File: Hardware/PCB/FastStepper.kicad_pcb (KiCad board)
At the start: 4 copper layers, 58 x 77.6 mm, 126 parts, among them IC1 FT232RL, IC10 THS4281DBVT, IC11 M74VHC1GT126DT1G, IC13 M74VHC1GT126DT1G, IC14 M74VHC1GT126DT1G, IC15 M74VHC1GT126DT1G, IC16 M74VHC1GT126DT1G, IC17 M74VHC1GT126DT1G, IC18 M74VHC1GT126DT1G, IC19 M74VHC1GT126DT1G, IC2 M74VHC1GT126DT1G, IC20 M74VHC1GT126DT1G, IC21 M74VHC1GT126DT1G, IC22 M74VHC1GT126DT1G, IC3 LP5907MFX-3.3, IC4 M74VHC1GT126DT1G, IC5 M74VHC1GT126DT1G, IC6 M74VHC1GT126DT1G, IC8 ATXMEGA32A4U, J1 USB_C_Receptacle, J2 AudioJack3_Ground_SwitchTR, J3 AudioJack3_Ground_SwitchTR, Q1 AO3401A, U1 74LVC1G157, U2 THVD1450D, U3 ADuM1201BR NOT NORMALLY STOCK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, X1 conn 1x5 2, X10 conn 1x3, X2 conn 1x5, X3 conn 1x2, X4 conn 1x3, X5 conn 1x5, X6 OSCILLATOR, X9 conn 1x5

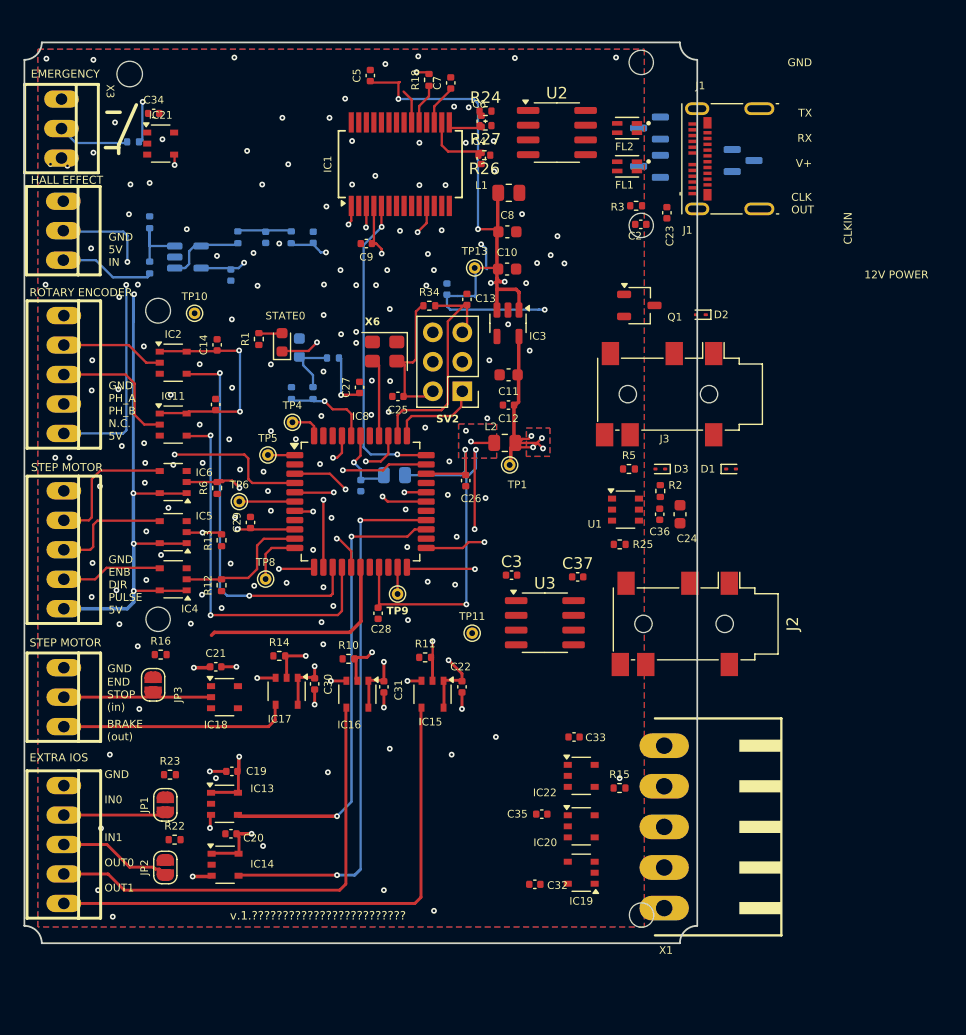
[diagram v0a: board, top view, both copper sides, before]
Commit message: FastStepper DRC=0
DRC=0
ainda não revisto com mais ninguém
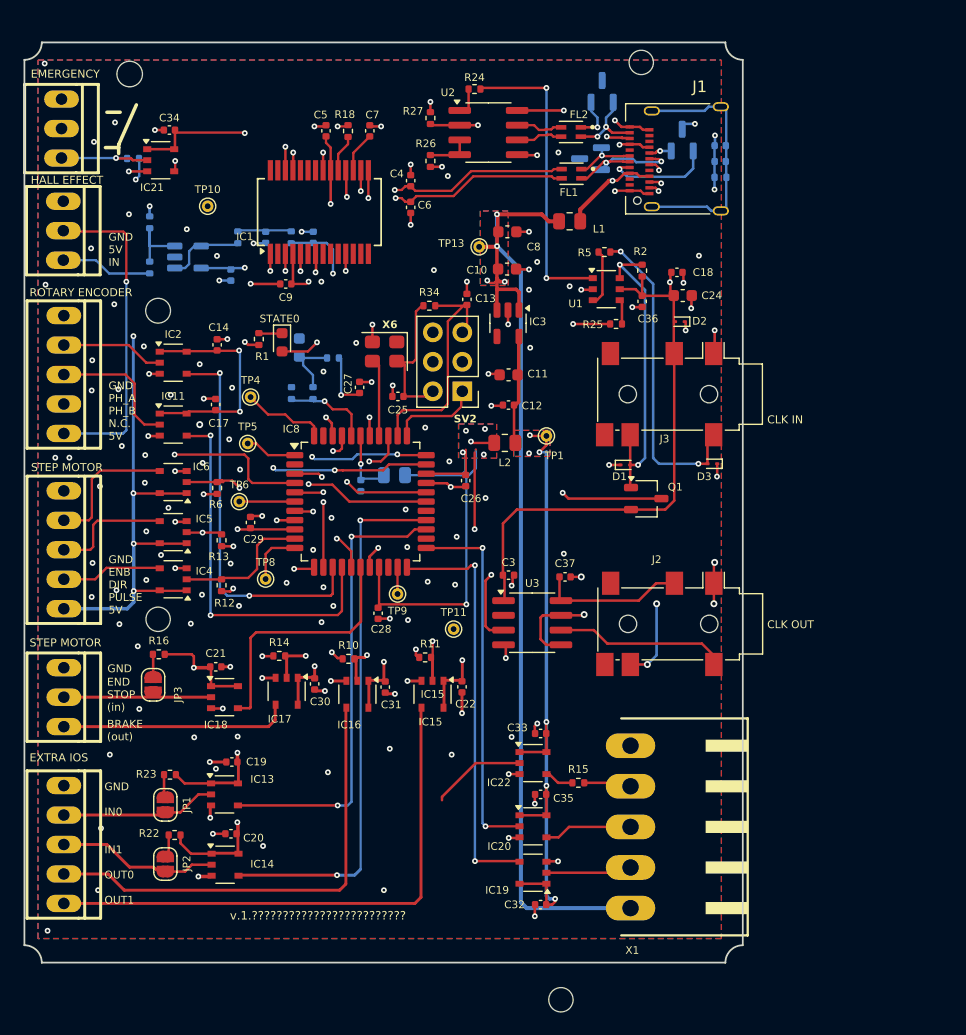
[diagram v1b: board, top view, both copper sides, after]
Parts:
- C18: moved to F.Cu
- C2, C23, R3: moved to B.Cu
- J1: footprint Connector_USB:USB_C_Receptacle_Molex_105450-0101 -> Connector_USB:USB_C_Receptacle_Amphenol_12401610E4-2A
- moved C18 19.9 mm to (175.8, 86.0), turned to 180 degrees
- moved U1 19.1 mm to (169.7, 87.5)
- moved R2 19.1 mm to (172.8, 85.8)
- moved R25 19.0 mm to (170.5, 90.5)
- moved C24 18.9 mm to (176.2, 88.0), turned to 0 degrees
- moved R5 18.8 mm to (169.5, 84.2)
- moved C36 18.4 mm to (172.8, 88.5)
- moved Q1 16.7 mm to (173.1, 105.5)
- moved C6 9.60 mm to (152.8, 80.4), turned to -90 degrees
- moved TP10 9.30 mm to (135.3, 80.3)
- moved D1 9.12 mm to (171.3, 102.6)
- moved C2 8.73 mm to (179.5, 76.4), turned to 180 degrees
- moved R18 8.26 mm to (147.4, 73.8)
- moved C7 8.11 mm to (149.3, 73.8)
- moved IC1 8.11 mm to (144.9, 80.8)
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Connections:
- net Net-(D3-A2) renamed /Clock stage/CLCK_IN
- net Net-(U3-VOB) renamed /Clock stage/CLCK_OUT
- C18 pad 2: Net-(D2-A2) -> VClk
- D2 pad 2: Net-(D2-A2) -> VClk
- D4 pad 1: /CC2 -> /CC1
- D4 pad 2: /CC1 -> /CC2
- FL1 pad 1: /USB_P -> /USB_N
- FL1 pad 2: /USB_2u_P -> /USB_2u_N
- FL1 pad 3: /USB_2u_N -> /USB_2u_P
- FL1 pad 4: /USB_N -> /USB_P
- J3 pad 3: Net-(D2-A2) -> VClk
- R27 pad 1: Net-(U2-~{RE}) -> ~{CLK_EN_USB}
- U2 pad 2: Net-(U2-~{RE}) -> ~{CLK_EN_USB}
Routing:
- net GND: track 12.9 -> 103.2 mm, vias 141 -> 150
- net VClk: track 0.00 -> 76.0 mm, vias 0 -> 3
- net +5V: track 245.0 -> 313.9 mm
- net ~{CLK_EN_USB}: track 0.00 -> 51.1 mm, vias 0 -> 3
- net GNDS: track 0.00 -> 42.8 mm, vias 0 -> 6
- net HARP_H2_RX: track 5.88 -> 35.3 mm, vias 1 -> 2
- net +3V3: track 272.8 -> 300.9 mm, vias 18 -> 21
- net /Clock stage/CLCK_IN: track 0.00 -> 27.6 mm, vias 0 -> 2
- net Net-(D1-A2): track 0.00 -> 26.8 mm, vias 0 -> 2
- net HARP_H2_TX: track 5.10 -> 31.8 mm, vias 1 -> 2
- net CLK_USB: track 0.00 -> 26.0 mm, vias 0 -> 2
- net Net-(J1-SHIELD): track 0.00 -> 21.2 mm
- net /USB_2u_P: track 3.43 -> 20.3 mm, vias 0 -> 2
- net /USB_CLCK_P: track 0.00 -> 16.4 mm, vias 0 -> 3
- net /USB_CLCK_N: track 0.00 -> 15.4 mm, vias 0 -> 3
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- added copper zone on B.Cu, net +5V
- added copper zone on F.Cu, net +5V
- added copper zone on In1.Cu, net +5V
- added copper zone on In2.Cu, net +5V
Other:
- board size 58 x 77.6 mm -> 61.9 x 83.6 mm
- board text added: "CLK IN"
- board text removed: "12V POWER"
- board text removed: "CLKIN"
- board text removed: "GND TX RX V+"

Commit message: ver comentarios no .txt
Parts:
- added J6: Keystone 8734, FastStepper PCBLib:Terminal_Block_Keystone_8734_1x01_Horizontal_Screw, F.Cu at (150.7, 131.6)
- added SC1: Pin_D4mm_hole2mm, FastStepper PCBLib:Pin_D4mm_hole2mm, F.Cu at (131.4, 67.5)
- added SC1: Pin_D4mm_hole2mm, FastStepper PCBLib:Pin_D4mm_hole2mm, F.Cu at (175.5, 146.0)
- added SC1: Pin_D4mm_hole2mm, FastStepper PCBLib:Pin_D4mm_hole2mm, F.Cu at (175.8, 107.6)
- added SC1: Pin_D4mm_hole2mm, FastStepper PCBLib:Pin_D4mm_hole2mm, F.Cu at (131.4, 116.6)
- added SC1: Pin_D4mm_hole2mm, FastStepper PCBLib:Pin_D4mm_hole2mm, F.Cu at (175.8, 67.5)
- added SC1: Pin_D4mm_hole2mm, FastStepper PCBLib:Pin_D4mm_hole2mm, F.Cu at (131.4, 146.0)
- moved JP3 0.81 mm to (131.0, 122.2)
- moved R16 0.58 mm to (131.1, 119.5)
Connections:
- IC22 pad 2: HARP_H2_CLOCK_OUT -> CLCK_OUT
- J2 pad 2: /Clock stage/CLCK_OUT -> CLCK_OUT
- U3 pad 6: /Clock stage/CLCK_OUT -> CLCK_OUT
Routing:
- net CLCK_OUT: track 0.00 -> 22.4 mm
- net /Clock stage/CLCK_OUT: track 14.2 -> 0.00 mm
- net HARP_H2_CLOCK_OUT: track 8.17 -> 0.00 mm
- net +3V3: track 300.9 -> 300.1 mm
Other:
- board size 61.9 x 83.6 mm -> 61.9 x 84.4 mm
- board text added: "5V"
- board text added: "DIR"
- board text added: "ENB"
- board text added: "IN"
- board text added: "IN0"
- board text added: "IN1"
- board text added: "N.C."
- board text added: "OUT0"
- board text added: "OUT1"
- board text added: "PH_A"
- board text added: "PH_B"
- board text added: "PULSE"
- board text removed: "GND 5V IN"
- board text removed: "GND ENB DIR PULSE 5V"
- board text removed: "GND IN0 IN1 OUT0 OUT1"
- board text removed: "GND PH_A PH_B N.C. 5V"

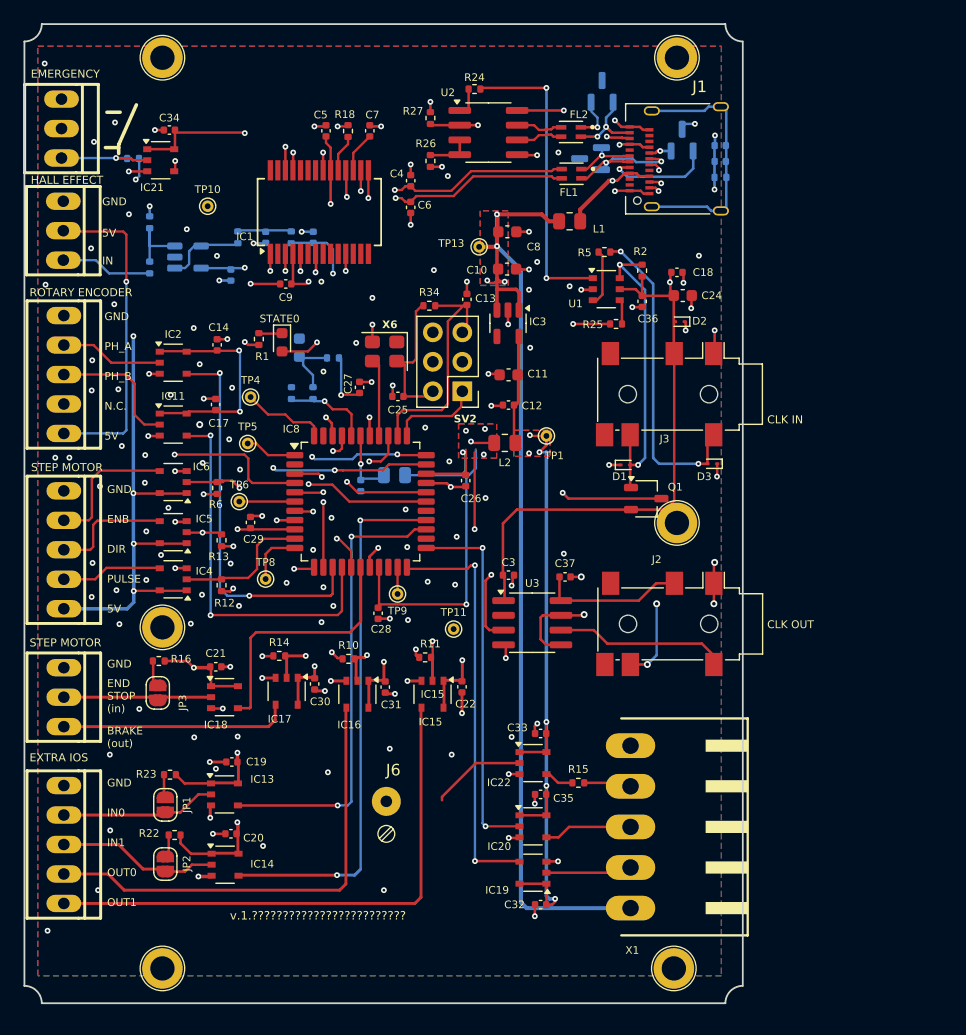
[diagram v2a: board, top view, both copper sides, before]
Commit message: DRC=0; mudanças faladas com Neurogears @12Junho OK
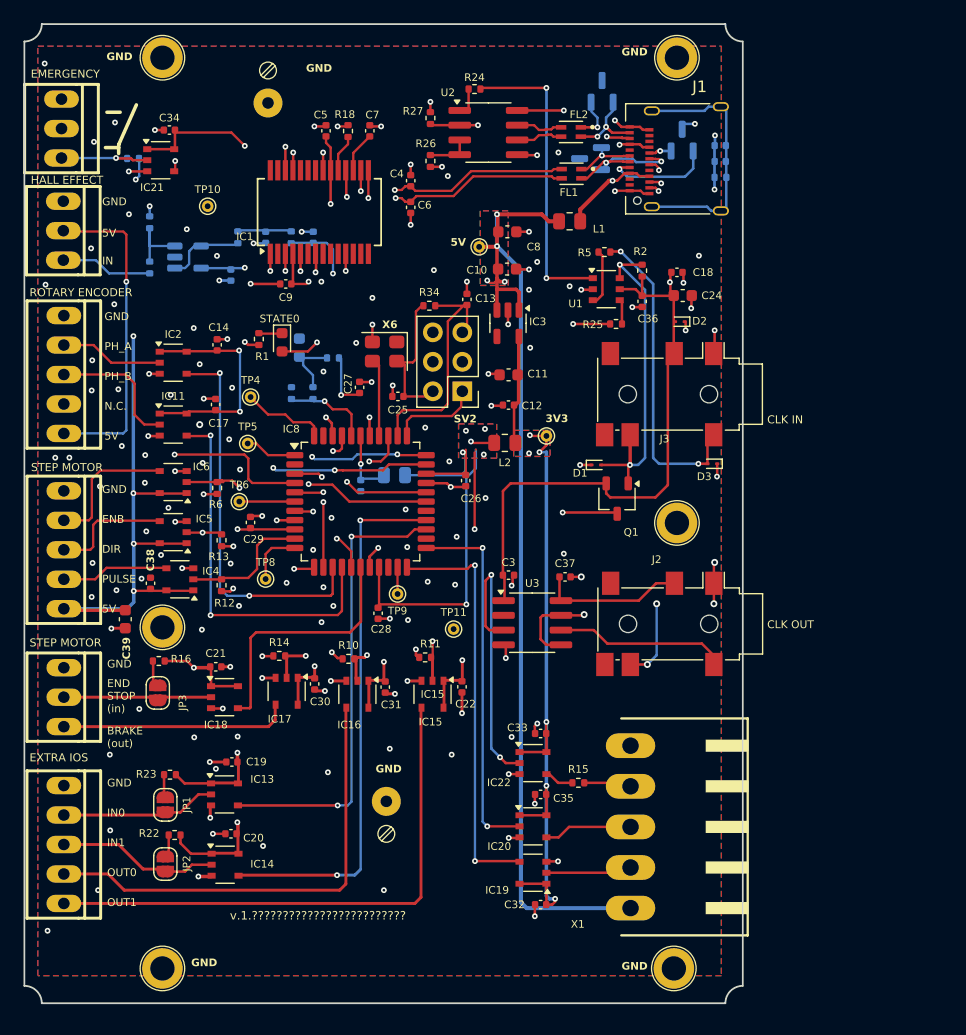
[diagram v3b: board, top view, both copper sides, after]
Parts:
- added C38: 100nF, Capacitor_SMD:C_0402_1005Metric, F.Cu at (130.4, 112.8)
- added C39: 4.7uF, Capacitor_SMD:C_0603_1608Metric, F.Cu at (128.2, 115.9)
- added J4: Keystone 8734, FastStepper PCBLib:Terminal_Block_Keystone_8734_1x01_Horizontal_Screw, F.Cu at (140.5, 71.4)
- moved D1 2.50 mm to (168.8, 102.6)
- moved Q1 2.50 mm to (170.6, 105.5), turned to -90 degrees
- moved IC4 0.57 mm to (132.9, 112.5)
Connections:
- IC22 pad 2: CLCK_OUT -> CLK_2u
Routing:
- net CLK_2u: track 55.8 -> 73.6 mm, vias 4 -> 5
- net CLCK_OUT: track 22.4 -> 14.2 mm
- net +5V: track 313.9 -> 319.8 mm
- net ~{CLK_EN_USB}: track 51.1 -> 48.8 mm
- net Net-(D1-A2): track 26.8 -> 28.9 mm
- net VClk: track 76.0 -> 78.0 mm
- net GND: track 103.2 -> 104.4 mm, vias 150 -> 149
- net +3V3: track 300.1 -> 299.5 mm
- net /IO stage/STEP_PULSE: track 8.63 -> 9.26 mm
- net U_STEP_PULSE: track 11.8 -> 11.3 mm
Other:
- board text added: "3V3"

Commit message: adicionados ficheiros Gerbers&Drills
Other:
- board text added: "FastStepper v.1.0"
- board text removed: "v.1.?????????????????????????"
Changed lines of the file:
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@@
 		(allow_soldermask_bridges_in_footprints no)
 		(tenting front back)
+		(aux_axis_origin 119.5011 149)
 		(pcbplotparams
 			(layerselection 0x00000000_00000000_55555555_5755f5ff)
-			(plot_on_all_layers_selection 0x00000000_00000000_00000000_00000000)
+			(plot_on_all_layers_selection 0x00000000_00000000_00000000_02000000)
 			(disableapertmacros no)
 			(usegerberextensions no)
@@
 			(plotframeref no)
 			(mode 1)
-			(useauxorigin no)
+			(useauxorigin yes)
 			(hpglpennumber 1)
 			(hpglpenspeed 20)
@@
 			(outputformat 1)
 			(mirror no)
-			(drillshape 1)
+			(drillshape 0)
 			(scaleselection 1)
-			(outputdirectory "")
+			(outputdirectory "Gerbers&Drills/")
 		)
 	)
@@
 		)
 	)
-	(gr_text "v.1.?????????????????????????"
-		(at 137.2141 141.8746 0)
+	(gr_text "FastStepper v.1.0"
+		(at 143.8 145.3 0)
 		(layer "F.SilkS")
 		(effects

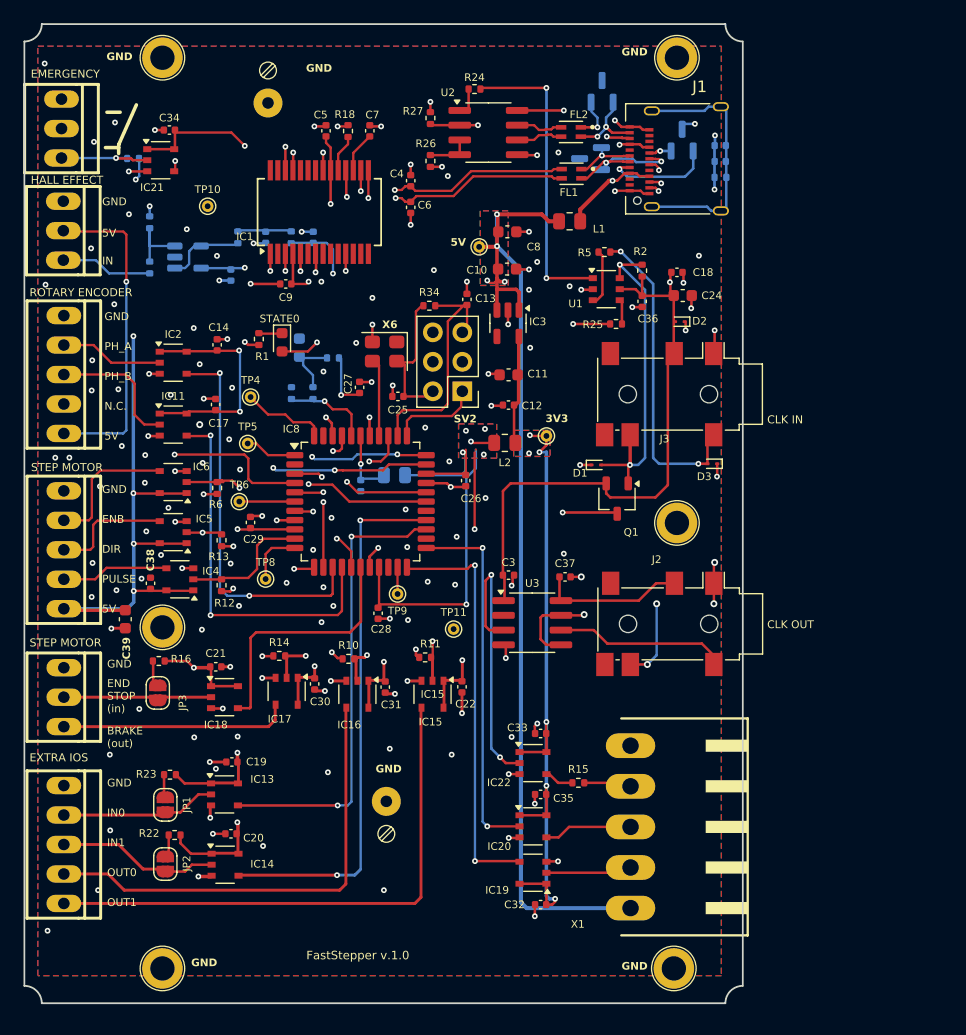
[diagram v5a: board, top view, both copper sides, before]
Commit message: MPN & OEPSPN concluded
concluded but not yet certified
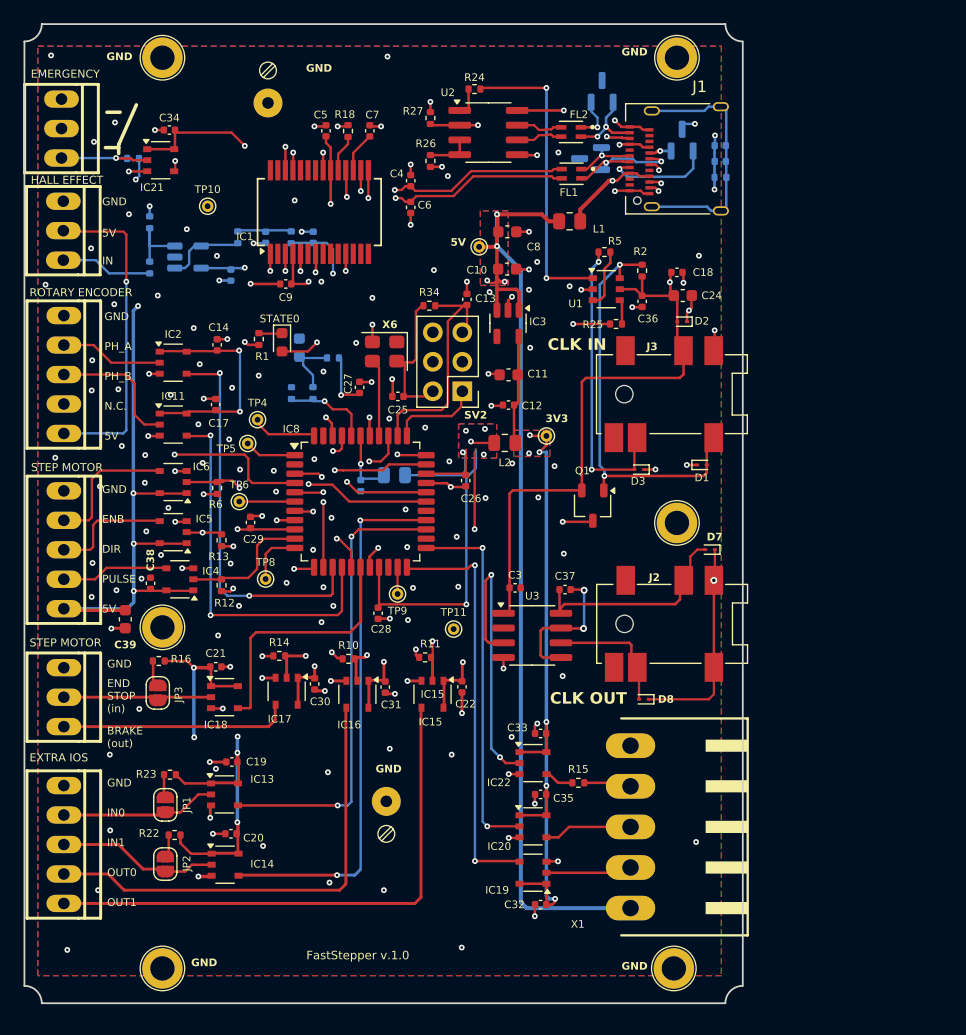
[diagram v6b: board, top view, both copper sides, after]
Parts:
- added D7: ESD9B3, Diode_SMD:D_SOD-923, F.Cu at (178.6, 109.9)
- added D8: ESD9B3, Diode_SMD:D_SOD-923, F.Cu at (172.9, 122.8)
- C41, C42: value 15nF 5% -> 15nF
- J2, J3: value AudioJack3_Ground_SwitchTR -> PJ-316A-6A; footprint Connector_Audio:Jack_3.5mm_PJ311_Horizontal -> FastStepper PCBLib:Jack_3.5mm_PJ316A_Horizontal
- U3: value ADuM1201BR NOT NORMALLY STOCKED -> ADUM1201BRZ
- moved D1 9.10 mm to (177.9, 102.6)
- moved D3 6.32 mm to (172.5, 103.0)
- moved Q1 2.18 mm to (168.5, 106.1)
- moved TP4 2.04 mm to (139.6, 98.7)
- moved C3 1.23 mm to (161.8, 113.2)
- moved C37 1.09 mm to (166.1, 113.3)
- moved U3 1.09 mm to (163.3, 117.3)
- moved D2 0.20 mm to (176.2, 90.2)
- turned R5 to 180 degrees
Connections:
- net CLCK_OUT renamed /Clock stage/CLCK_OUT
- net Net-(D1-A2) renamed /Clock stage/~{CLCK_DET}
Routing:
- net /Clock stage/~{CLCK_DET}: track 28.9 -> 36.8 mm
- net Net-(D7-A2): track 12.3 -> 18.5 mm
- net /Clock stage/CLCK_OUT: track 14.2 -> 11.1 mm
- net CLK_2u: track 73.6 -> 75.4 mm
- net /Clock stage/CLCK_IN: track 27.6 -> 25.9 mm
- net Net-(IC8-PA4/ADC4): track 7.21 -> 5.57 mm
- net ~{CLK_EN_USB}: track 48.8 -> 47.5 mm
- net +5V: track 319.8 -> 321.0 mm
- net GNDS: track 42.8 -> 41.8 mm, vias 6 -> 3
- net Net-(IC8-PR1/XTAL1): track 6.23 -> 7.03 mm
- net FTDI_RTS: track 31.6 -> 32.1 mm
- net GND: track 104.4 -> 104.2 mm, vias 149 -> 161
- net (no net): vias 1 -> 0
